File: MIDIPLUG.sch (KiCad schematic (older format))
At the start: 28 parts, among them J1 Wavetable Connector, U1 LP2985-3.3, U2 SAM2695, U3 4050, Y1 12Mhz

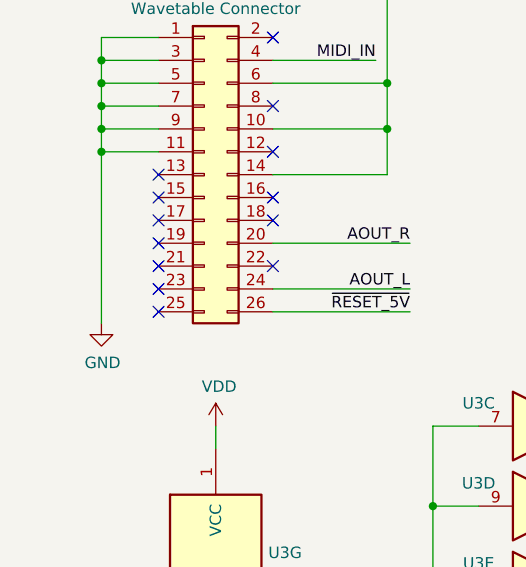
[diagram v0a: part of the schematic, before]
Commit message: Connect GNDA
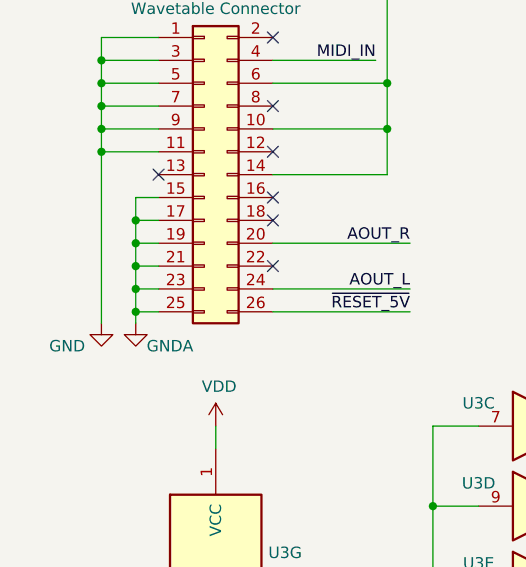
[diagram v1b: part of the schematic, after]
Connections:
- net GNDA: now also J1.15 (Pin_15), J1.17 (Pin_17), J1.19 (Pin_19), J1.21 (Pin_21), J1.23 (Pin_23), J1.25 (Pin_25)
- no-connect marks 28 -> 22
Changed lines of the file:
@@
 P 950 5500
 F 0 "#PWR0112" H 950 5250 50  0001 C CNN
-F 1 "GND" H 955 5327 50  0000 C CNN
+F 1 "GND" H 800 5400 50  0000 C CNN
 F 2 "" H 950 5500 50  0001 C CNN
 F 3 "" H 950 5500 50  0001 C CNN
@@
 	950  4750 950  5500
 NoConn ~ 1200 4850
-NoConn ~ 1200 4950
-NoConn ~ 1200 5050
-NoConn ~ 1200 5150
-NoConn ~ 1200 5250
-NoConn ~ 1200 5350
-NoConn ~ 1200 5450
 $Comp
 L power:VCC #PWR0123
@@
 Wire Wire Line
 	900  2550 1250 2550
+$Comp
+L power:GNDA #PWR?
+U 1 1 60E2122D
+P 1100 5500
+F 0 "#PWR?" H 1100 5250 50  0001 C CNN
+F 1 "GNDA" H 1250 5400 50  0000 C CNN
+F 2 "" H 1100 5500 50  0001 C CNN
+F 3 "" H 1100 5500 50  0001 C CNN
+	1    1100 5500
+	1    0    0    -1
+$EndComp
+Wire Wire Line
+	1200 4950 1100 4950
+Wire Wire Line
+	1100 4950 1100 5050
+Wire Wire Line
+	1200 5050 1100 5050
+Connection ~ 1100 5050
+Wire Wire Line
+	1100 5050 1100 5150
+Wire Wire Line
+	1200 5150 1100 5150
+Connection ~ 1100 5150
+Wire Wire Line
+	1100 5150 1100 5250
+Wire Wire Line
+	1200 5250 1100 5250
+Connection ~ 1100 5250
+Wire Wire Line
+	1100 5250 1100 5350
+Wire Wire Line
+	1200 5350 1100 5350
+Connection ~ 1100 5350
+Wire Wire Line
+	1100 5350 1100 5450
+Wire Wire Line
+	1200 5450 1100 5450
+Connection ~ 1100 5450
+Wire Wire Line
+	1100 5450 1100 5500
 $EndSCHEMATC
